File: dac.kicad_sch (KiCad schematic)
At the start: 27 parts, among them U13 L78L05_SOT89, U14 AK4454

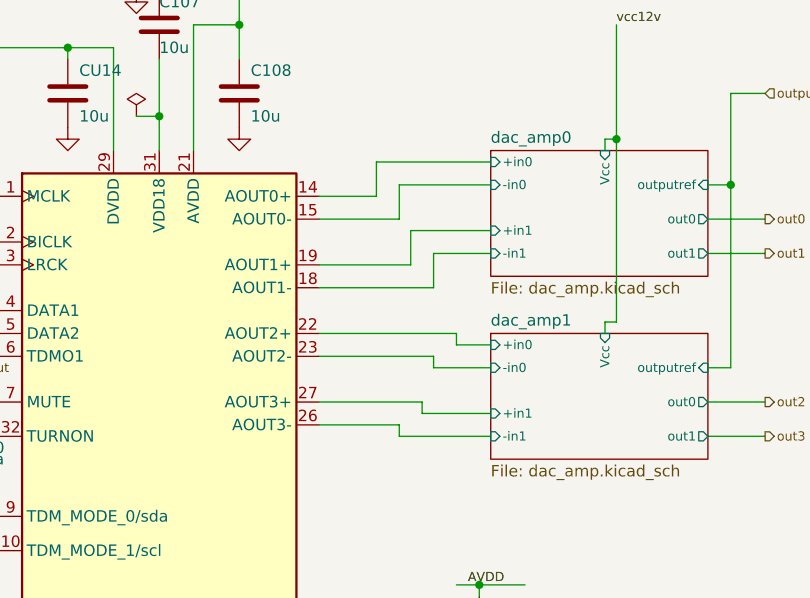
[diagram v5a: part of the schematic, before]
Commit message: routing...
+ swap around dac channels, otherwise routing was crazy
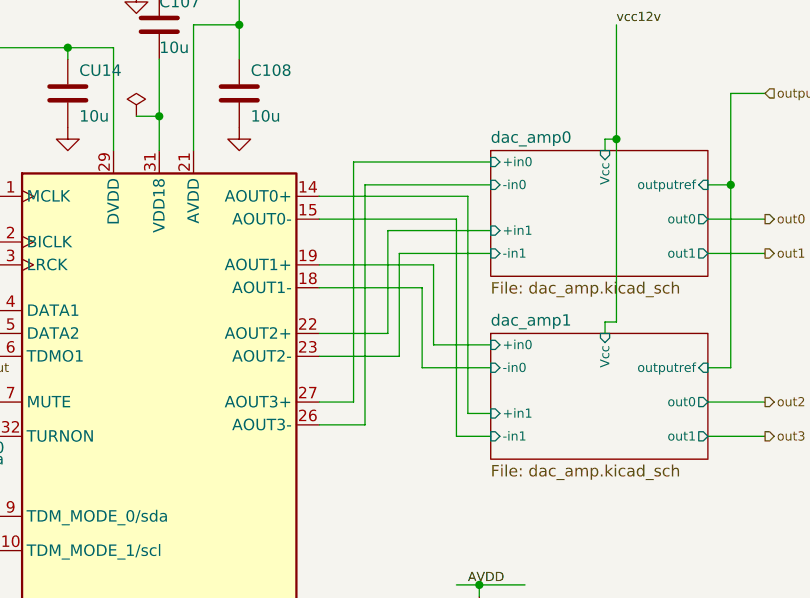
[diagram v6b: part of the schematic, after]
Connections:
- net dac_amp0/+in0: now also U14.27 (AOUT3+); no longer U14.14 (AOUT0+)
- net dac_amp0/+in1: now also U14.22 (AOUT2+); no longer U14.19 (AOUT1+)
- net dac_amp0/-in0: now also U14.26 (AOUT3-); no longer U14.15 (AOUT0-)
- net dac_amp0/-in1: now also U14.23 (AOUT2-); no longer U14.18 (AOUT1-)
- net dac_amp1/+in0: now also U14.19 (AOUT1+); no longer U14.22 (AOUT2+)
- net dac_amp1/+in1: now also U14.14 (AOUT0+); no longer U14.27 (AOUT3+)
- net dac_amp1/-in0: now also U14.18 (AOUT1-); no longer U14.23 (AOUT2-)
- net dac_amp1/-in1: now also U14.15 (AOUT0-); no longer U14.26 (AOUT3-)
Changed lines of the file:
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@@
+	(wire
+		(pts
+			(xy 156.21 83.82) (xy 160.02 83.82)
+		)
+		(stroke
+			(width 0)
+			(type default)
+		)
+	)
 	(wire
 		(pts
@@
 	(wire
 		(pts
-			(xy 168.91 67.31) (xy 175.26 67.31)
-		)
-		(stroke
-			(width 0)
-			(type default)
-		)
-	)
-	(wire
-		(pts
 			(xy 147.32 45.72) (xy 147.32 41.91)
 		)
@@
 	(wire
 		(pts
+			(xy 168.91 77.47) (xy 175.26 77.47)
+		)
+		(stroke
+			(width 0)
+			(type default)
+		)
+	)
+	(wire
+		(pts
 			(xy 95.25 92.71) (xy 96.52 92.71)
 		)
@@
 	(wire
 		(pts
+			(xy 172.72 85.09) (xy 175.26 85.09)
+		)
+		(stroke
+			(width 0)
+			(type default)
+		)
+	)
+	(wire
+		(pts
 			(xy 114.3 115.57) (xy 120.65 115.57)
 		)
@@
 	(wire
 		(pts
+			(xy 167.64 80.01) (xy 175.26 80.01)
+		)
+		(stroke
+			(width 0)
+			(type default)
+		)
+	)
+	(wire
+		(pts
 			(xy 187.96 76.2) (xy 187.96 74.93)
 		)
@@
 	(wire
 		(pts
-			(xy 175.26 80.01) (xy 168.91 80.01)
+			(xy 171.45 87.63) (xy 175.26 87.63)
 		)
 		(stroke
@@
 	(wire
 		(pts
-			(xy 165.1 63.5) (xy 165.1 59.69)
-		)
-		(stroke
-			(width 0)
-			(type default)
-		)
-	)
-	(wire
-		(pts
 			(xy 99.06 100.33) (xy 99.06 107.95)
 		)
@@
 	(wire
 		(pts
-			(xy 167.64 85.09) (xy 167.64 83.82)
+			(xy 156.21 60.96) (xy 172.72 60.96)
 		)
 		(stroke
@@
 	(wire
 		(pts
-			(xy 166.37 68.58) (xy 156.21 68.58)
-		)
-		(stroke
-			(width 0)
-			(type default)
-		)
-	)
-	(wire
-		(pts
 			(xy 157.48 113.03) (xy 157.48 120.65)
 		)
@@
 	(wire
 		(pts
+			(xy 168.91 68.58) (xy 168.91 77.47)
+		)
+		(stroke
+			(width 0)
+			(type default)
+		)
+	)
+	(wire
+		(pts
 			(xy 113.03 83.82) (xy 120.65 83.82)
 		)
@@
 	(wire
 		(pts
-			(xy 175.26 87.63) (xy 165.1 87.63)
-		)
-		(stroke
-			(width 0)
-			(type default)
-		)
-	)
-	(wire
-		(pts
-			(xy 165.1 87.63) (xy 165.1 86.36)
-		)
-		(stroke
-			(width 0)
-			(type default)
-		)
-	)
-	(wire
-		(pts
 			(xy 115.57 73.66) (xy 120.65 73.66)
 		)
@@
 	(wire
 		(pts
-			(xy 168.91 80.01) (xy 168.91 78.74)
-		)
-		(stroke
-			(width 0)
-			(type default)
-		)
-	)
-	(wire
-		(pts
 			(xy 187.96 74.93) (xy 189.23 74.93)
 		)
@@
 	(wire
 		(pts
-			(xy 175.26 64.77) (xy 166.37 64.77)
-		)
-		(stroke
-			(width 0)
-			(type default)
-		)
-	)
-	(wire
-		(pts
 			(xy 138.43 52.07) (xy 138.43 55.88)
 		)
@@
 	(wire
 		(pts
-			(xy 175.26 85.09) (xy 167.64 85.09)
-		)
-		(stroke
-			(width 0)
-			(type default)
-		)
-	)
-	(wire
-		(pts
 			(xy 99.06 100.33) (xy 101.6 100.33)
 		)
@@
 	(wire
 		(pts
-			(xy 171.45 77.47) (xy 171.45 76.2)
-		)
-		(stroke
-			(width 0)
-			(type default)
-		)
-	)
-	(wire
-		(pts
-			(xy 162.56 60.96) (xy 156.21 60.96)
-		)
-		(stroke
-			(width 0)
-			(type default)
-		)
-	)
-	(wire
-		(pts
 			(xy 189.23 54.61) (xy 189.23 74.93)
 		)
@@
 	(wire
 		(pts
-			(xy 165.1 86.36) (xy 156.21 86.36)
-		)
-		(stroke
-			(width 0)
-			(type default)
-		)
-	)
-	(wire
-		(pts
 			(xy 99.06 111.76) (xy 101.6 111.76)
 		)
@@
 	(wire
 		(pts
-			(xy 175.26 77.47) (xy 171.45 77.47)
+			(xy 165.1 67.31) (xy 175.26 67.31)
 		)
 		(stroke
@@
 	(wire
 		(pts
+			(xy 156.21 78.74) (xy 165.1 78.74)
+		)
+		(stroke
+			(width 0)
+			(type default)
+		)
+	)
+	(wire
+		(pts
+			(xy 156.21 86.36) (xy 161.29 86.36)
+		)
+		(stroke
+			(width 0)
+			(type default)
+		)
+	)
+	(wire
+		(pts
 			(xy 201.93 49.53) (xy 201.93 59.69)
 		)
@@
 	(wire
 		(pts
-			(xy 167.64 83.82) (xy 156.21 83.82)
+			(xy 161.29 59.69) (xy 175.26 59.69)
 		)
 		(stroke
@@
 	(wire
 		(pts
+			(xy 167.64 71.12) (xy 167.64 80.01)
+		)
+		(stroke
+			(width 0)
+			(type default)
+		)
+	)
+	(wire
+		(pts
+			(xy 163.83 76.2) (xy 163.83 64.77)
+		)
+		(stroke
+			(width 0)
+			(type default)
+		)
+	)
+	(wire
+		(pts
+			(xy 165.1 78.74) (xy 165.1 67.31)
+		)
+		(stroke
+			(width 0)
+			(type default)
+		)
+	)
+	(wire
+		(pts
 			(xy 99.06 123.19) (xy 99.06 119.38)
 		)
@@
 	(wire
 		(pts
+			(xy 156.21 71.12) (xy 167.64 71.12)
+		)
+		(stroke
+			(width 0)
+			(type default)
+		)
+	)
+	(wire
+		(pts
 			(xy 102.87 27.94) (xy 102.87 29.21)
 		)
@@
 	(wire
 		(pts
+			(xy 156.21 68.58) (xy 168.91 68.58)
+		)
+		(stroke
+			(width 0)
+			(type default)
+		)
+	)
+	(wire
+		(pts
 			(xy 95.25 92.71) (xy 95.25 95.25)
 		)
@@
 	(wire
 		(pts
+			(xy 156.21 76.2) (xy 163.83 76.2)
+		)
+		(stroke
+			(width 0)
+			(type default)
+		)
+	)
+	(wire
+		(pts
 			(xy 199.39 63.5) (xy 205.74 63.5)
 		)
@@
 	(wire
 		(pts
-			(xy 168.91 78.74) (xy 156.21 78.74)
-		)
-		(stroke
-			(width 0)
-			(type default)
-		)
-	)
-	(wire
-		(pts
 			(xy 156.21 118.11) (xy 158.75 118.11)
 		)
@@
 	(wire
 		(pts
-			(xy 162.56 57.15) (xy 162.56 60.96)
+			(xy 172.72 60.96) (xy 172.72 85.09)
+		)
+		(stroke
+			(width 0)
+			(type default)
+		)
+	)
+	(wire
+		(pts
+			(xy 163.83 64.77) (xy 175.26 64.77)
 		)
 		(stroke
@@
 	(wire
 		(pts
-			(xy 171.45 76.2) (xy 156.21 76.2)
-		)
-		(stroke
-			(width 0)
-			(type default)
-		)
-	)
-	(wire
-		(pts
 			(xy 107.95 87.63) (xy 120.65 87.63)
 		)
@@
 	(wire
 		(pts
+			(xy 161.29 86.36) (xy 161.29 59.69)
+		)
+		(stroke
+			(width 0)
+			(type default)
+		)
+	)
+	(wire
+		(pts
 			(xy 199.39 87.63) (xy 205.74 87.63)
 		)
@@
 	(wire
 		(pts
-			(xy 168.91 71.12) (xy 168.91 67.31)
-		)
-		(stroke
-			(width 0)
-			(type default)
-		)
-	)
-	(wire
-		(pts
 			(xy 147.32 27.94) (xy 127 27.94)
 		)
@@
 	(wire
 		(pts
-			(xy 175.26 57.15) (xy 162.56 57.15)
+			(xy 160.02 57.15) (xy 175.26 57.15)
+		)
+		(stroke
+			(width 0)
+			(type default)
+		)
+	)
+	(wire
+		(pts
+			(xy 171.45 63.5) (xy 171.45 87.63)
 		)
 		(stroke
@@
 	(wire
 		(pts
-			(xy 166.37 64.77) (xy 166.37 68.58)
-		)
-		(stroke
-			(width 0)
-			(type default)
-		)
-	)
-	(wire
-		(pts
-			(xy 165.1 59.69) (xy 175.26 59.69)
-		)
-		(stroke
-			(width 0)
-			(type default)
-		)
-	)
-	(wire
-		(pts
-			(xy 156.21 71.12) (xy 168.91 71.12)
+			(xy 156.21 63.5) (xy 171.45 63.5)
 		)
 		(stroke
@@
 	(wire
 		(pts
-			(xy 156.21 63.5) (xy 165.1 63.5)
-		)
-		(stroke
+			(xy 160.02 83.82) (xy 160.02 57.15)
+		)
+		(stroke

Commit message: fill in some part numbers
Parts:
- U13: PN (none) -> ua78l05acpke6
- U14: PN (none) -> AK4454VN
- s24, s38, s40: now left out of the parts list
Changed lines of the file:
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@@
 		(unit 1)
 		(exclude_from_sim no)
-		(in_bom yes)
+		(in_bom no)
 		(on_board yes)
 		(dnp no)
@@
 		(unit 1)
 		(exclude_from_sim no)
-		(in_bom yes)
+		(in_bom no)
 		(on_board yes)
 		(dnp no)
@@
 			)
 		)
+		(property "PN" "ua78l05acpke6"
+			(at 116.84 27.94 0)
+			(effects
+				(font
+					(size 1.27 1.27)
+				)
+				(hide yes)
+			)
+		)
 		(pin "1"
 		)
@@
 		(unit 1)
 		(exclude_from_sim no)
-		(in_bom yes)
+		(in_bom no)
 		(on_board yes)
 		(dnp no)
@@
 			(at 138.43 93.98 0)
 			(effects
+				(font
+					(size 1.27 1.27)
+				)
+				(hide yes)
+			)
+		)
+		(property "PN" "AK4454VN"
+			(at 138.43 93.98 0)
+			(effects

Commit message: work on bugs...
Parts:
- C109: value 1u -> 10u
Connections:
- net 3V3: no longer R145.1
- new net pg: R145.1
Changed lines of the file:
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@@
 	)
 	(junction
-		(at 99.06 95.25)
-		(diameter 0)
-		(color 0 0 0 0)
-	)
-	(junction
 		(at 128.27 44.45)
 		(diameter 0)
@@
 	(wire
 		(pts
-			(xy 99.06 87.63) (xy 99.06 95.25)
-		)
-		(stroke
-			(width 0)
-			(type default)
-		)
-	)
-	(wire
-		(pts
 			(xy 110.49 68.58) (xy 120.65 68.58)
 		)
@@
 	(wire
 		(pts
+			(xy 88.9 87.63) (xy 102.87 87.63)
+		)
+		(stroke
+			(width 0)
+			(type default)
+		)
+	)
+	(wire
+		(pts
 			(xy 95.25 92.71) (xy 95.25 95.25)
 		)
@@
 	(wire
 		(pts
-			(xy 99.06 87.63) (xy 102.87 87.63)
-		)
-		(stroke
-			(width 0)
-			(type default)
-		)
-	)
-	(wire
-		(pts
 			(xy 189.23 41.91) (xy 189.23 54.61)
 		)
@@
 		)
 	)
+	(hierarchical_label "pg"
+		(shape input)
+		(at 88.9 87.63 180)
+		(fields_autoplaced yes)
+		(effects
+			(font
+				(size 1.016 1.016)
+			)
+			(justify right)
+		)
+	)
 	(hierarchical_label "out1"
 		(shape output)
@@
 			)
 		)
-		(property "Value" "1u"
+		(property "Value" "10u"
 			(at 165.1 116.84 0)
 			(effects
